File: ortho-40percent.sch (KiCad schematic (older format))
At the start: 28 parts, among them J1 USB-C_Receptacle-24, SW1 SW_NO_4-Pin, U1 U_TPD4E05U06DQAR, U2 U_ATmega32u4-MU, Y1 XTAL_4Lead

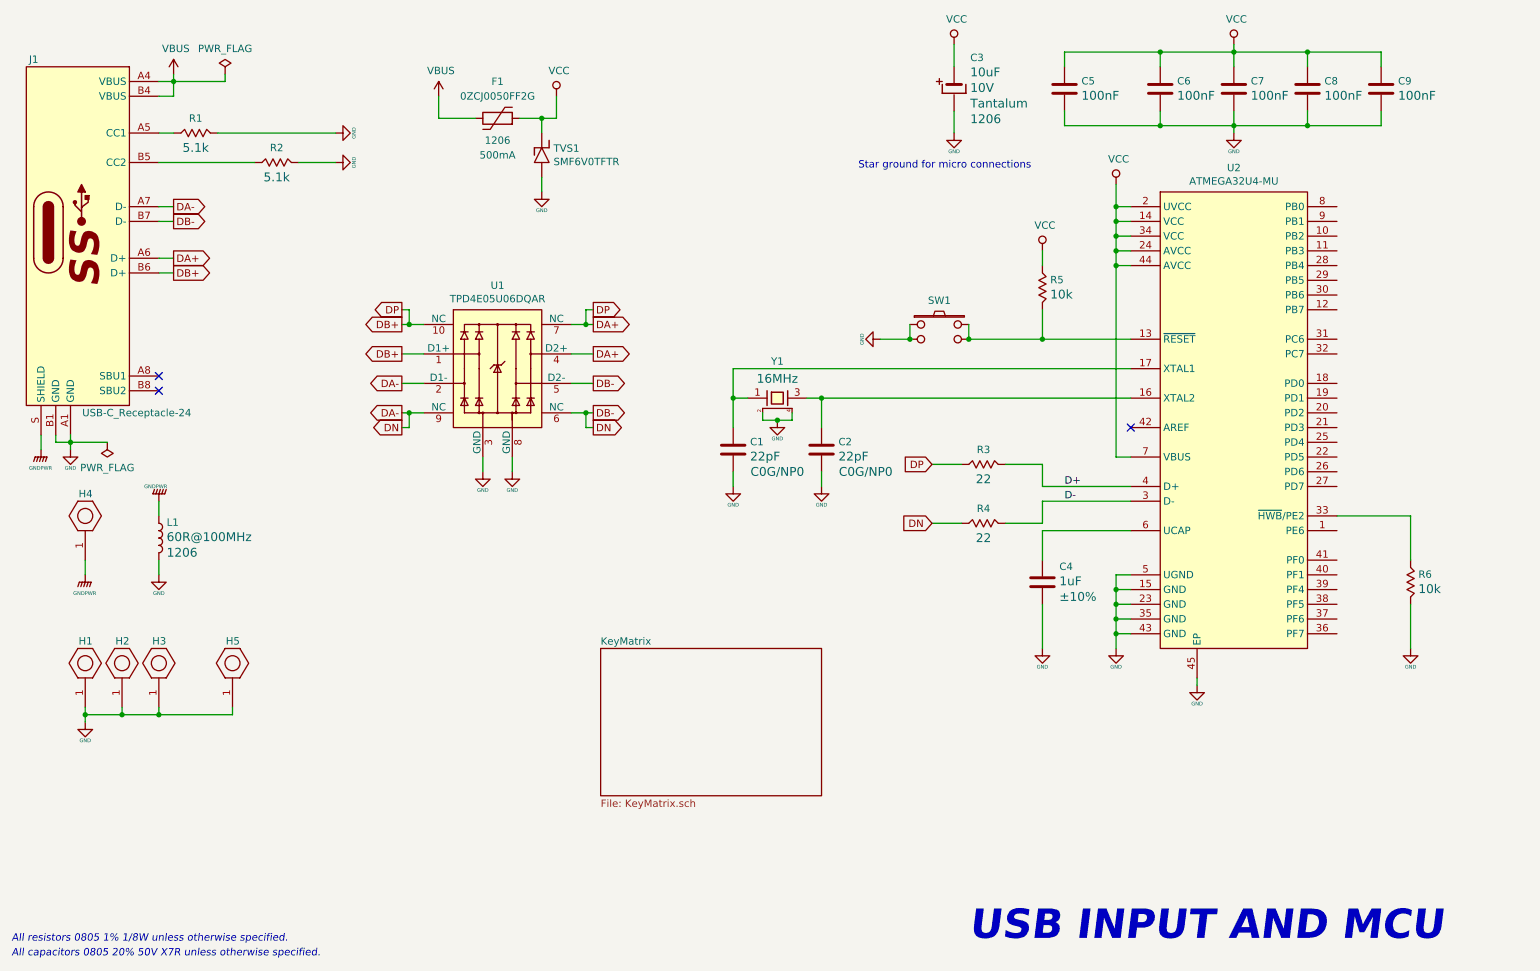
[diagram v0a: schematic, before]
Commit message: Routing Finished
All connections routed. Focusing on cleaning up for length optimization and minimal bottom plane cutting.
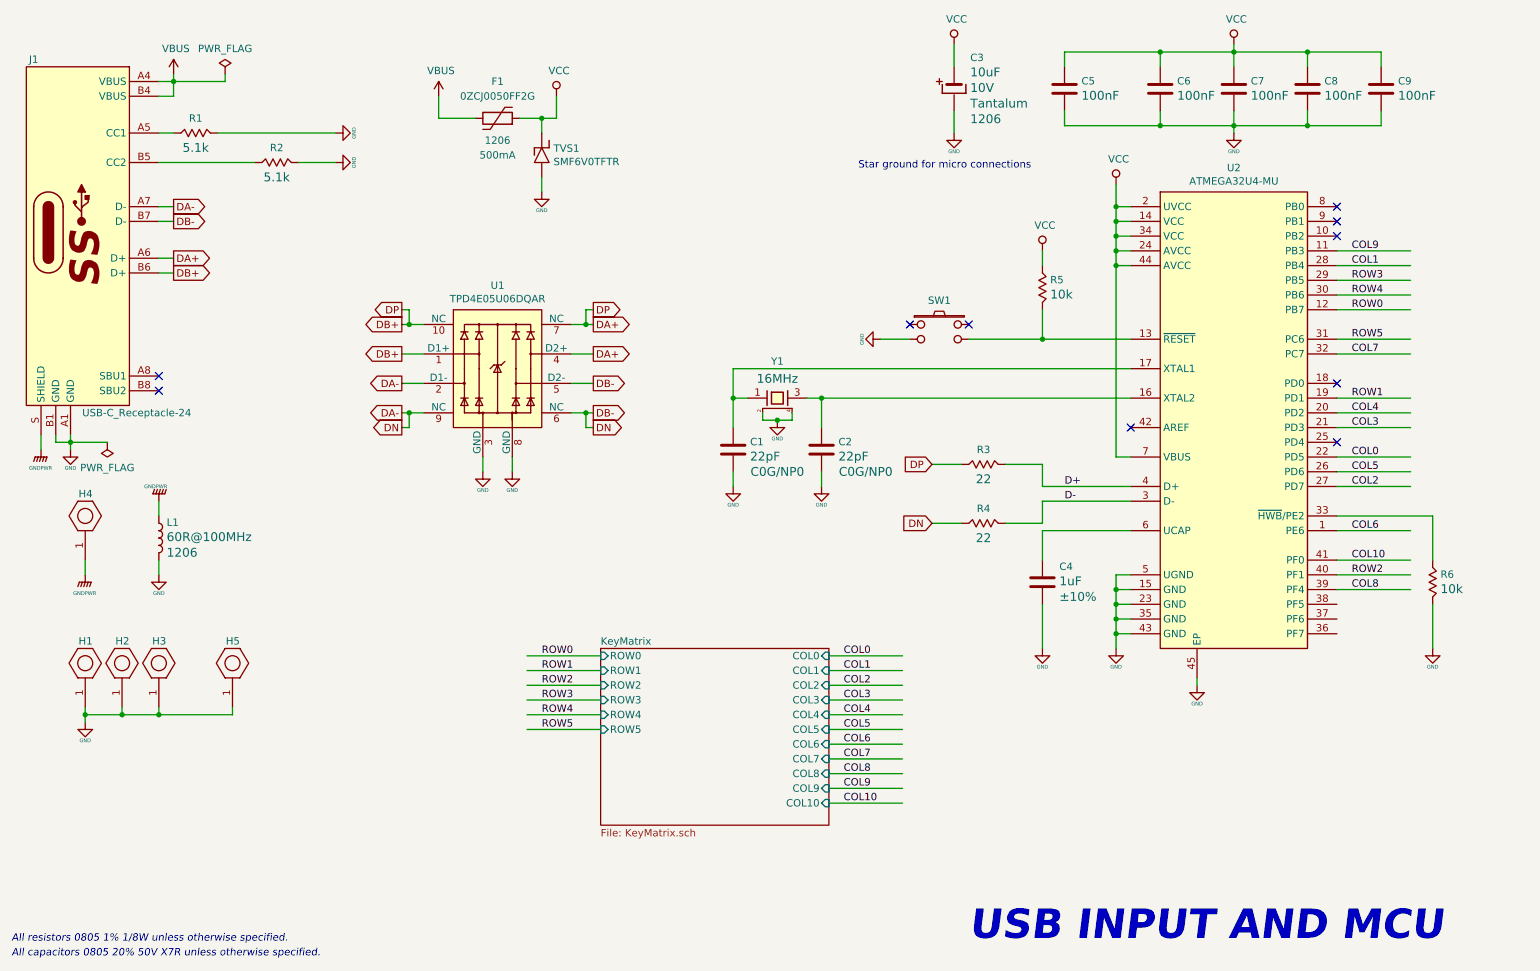
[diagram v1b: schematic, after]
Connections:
- net labels added: COL0, COL1, COL10, COL2, COL3, COL4, COL5, COL6, COL7, COL8, COL9, ROW0, ROW1, ROW2, ROW3, ROW4, ROW5
- wire segments 139 -> 171
- no-connect marks 3 -> 10
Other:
- moved on the sheet: R6
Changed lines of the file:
@@
 L master-vampire_General:R R6
 U 1 1 5F26A1E8
-P 10500 4550
-F 0 "R6" V 10447 4603 50  0000 L CNN
-F 1 "R" H 10500 4800 50  0001 C CNN
-F 2 "ortho-40percent:R_0805" H 10500 4620 50  0001 C CNN
-F 3 "" V 10500 4550 50  0000 C CNN
-F 4 "10k" V 10546 4603 60  0000 L CNN "Resistance"
-F 5 "1/8W" H 10900 4350 60  0001 C CNN "Power"
-F 6 "0805" H 10550 4350 60  0001 C CNN "Package"
-F 7 "1%" H 10800 4450 60  0001 C CNN "Tolerance"
-F 8 "RC0805FR-0710KL" H 11000 5150 50  0001 C CNN "MPN"
-F 9 "Yageo" H 11100 5250 50  0001 C CNN "Manufacturer"
-F 10 "DigiKey" H 11200 5350 50  0001 C CNN "Supplier"
-F 11 "311-10.0KCRCT-ND" H 11300 5450 50  0001 C CNN "Supplier PN"
-	1    10500 4550
+P 10650 4550
+F 0 "R6" V 10597 4603 50  0000 L CNN
+F 1 "R" H 10650 4800 50  0001 C CNN
+F 2 "ortho-40percent:R_0805" H 10650 4620 50  0001 C CNN
+F 3 "" V 10650 4550 50  0000 C CNN
+F 4 "10k" V 10696 4603 60  0000 L CNN "Resistance"
+F 5 "1/8W" H 11050 4350 60  0001 C CNN "Power"
+F 6 "0805" H 10700 4350 60  0001 C CNN "Package"
+F 7 "1%" H 10950 4450 60  0001 C CNN "Tolerance"
+F 8 "RC0805FR-0710KL" H 11150 5150 50  0001 C CNN "MPN"
+F 9 "Yageo" H 11250 5250 50  0001 C CNN "Manufacturer"
+F 10 "DigiKey" H 11350 5350 50  0001 C CNN "Supplier"
+F 11 "311-10.0KCRCT-ND" H 11450 5450 50  0001 C CNN "Supplier PN"
+	1    10650 4550
 	0    1    1    0
 $EndComp
@@
 L power:GND #PWR024
 U 1 1 5F273643
-P 10500 5000
-F 0 "#PWR024" H 10500 4750 50  0001 C CNN
-F 1 "GND" H 10500 4875 25  0000 C CNN
-F 2 "" H 10500 5000 50  0001 C CNN
-F 3 "" H 10500 5000 50  0001 C CNN
-	1    10500 5000
-	1    0    0    -1
-$EndComp
-Wire Wire Line
-	10000 4100 10500 4100
-Wire Wire Line
-	10500 4100 10500 4400
-Wire Wire Line
-	10500 4700 10500 5000
+P 10650 5000
+F 0 "#PWR024" H 10650 4750 50  0001 C CNN
+F 1 "GND" H 10650 4875 25  0000 C CNN
+F 2 "" H 10650 5000 50  0001 C CNN
+F 3 "" H 10650 5000 50  0001 C CNN
+	1    10650 5000
+	1    0    0    -1
+$EndComp
+Wire Wire Line
+	10650 4100 10650 4400
+Wire Wire Line
+	10650 4700 10650 5000
 Wire Wire Line
 	8600 4200 8000 4200
@@
 	5900 3100 8600 3100
 NoConn ~ 8600 3500
-Wire Wire Line
-	8000 2900 7500 2900
-Connection ~ 8000 2900
 $Comp
 L power:GND #PWR016
@@
 	0    1    1    0
 $EndComp
-Wire Wire Line
-	6900 2900 7100 2900
-Wire Wire Line
-	7500 2800 7500 2900
-Connection ~ 7500 2900
-Wire Wire Line
-	7100 2800 7100 2900
-Connection ~ 7100 2900
 $Comp
 L power:VCC #PWR022
@@
 	7400 1050 7400 900
 $Sheet
-S 5000 5000 1500 1000
+S 5000 5000 1550 1200
 U 5F33A928
 F0 "KeyMatrix" 50
 F1 "KeyMatrix.sch" 50
+F2 "ROW0" I L 5000 5050 50
+F3 "ROW1" I L 5000 5150 50
+F4 "ROW2" I L 5000 5250 50
+F5 "ROW3" I L 5000 5350 50
+F6 "ROW4" I L 5000 5450 50
+F7 "ROW5" I L 5000 5550 50
+F8 "COL0" I R 6550 5050 50
+F9 "COL1" I R 6550 5150 50
+F10 "COL2" I R 6550 5250 50
+F11 "COL3" I R 6550 5350 50
+F12 "COL4" I R 6550 5450 50
+F13 "COL5" I R 6550 5550 50
+F14 "COL6" I R 6550 5650 50
+F15 "COL7" I R 6550 5750 50
+F16 "COL8" I R 6550 5850 50
+F17 "COL9" I R 6550 5950 50
+F18 "COL10" I R 6550 6050 50
 $EndSheet
 $Comp
@@
 Wire Wire Line
 	1650 3600 1400 3600
+Wire Wire Line
+	10000 2600 10500 2600
+Wire Wire Line
+	10500 2700 10000 2700
+Wire Wire Line
+	10000 2900 10500 2900
+Wire Wire Line
+	10000 3900 10500 3900
+Wire Wire Line
+	10500 3300 10000 3300
+Wire Wire Line
+	10000 3400 10500 3400
+Wire Wire Line
+	10500 3500 10000 3500
+Wire Wire Line
+	10000 3800 10500 3800
+Wire Wire Line
+	10500 4500 10000 4500
+Wire Wire Line
+	10000 3000 10500 3000
+Text Label 10100 2700 0    50   ~ 0
+ROW0
+Text Label 10100 3300 0    50   ~ 0
+ROW1
+Text Label 10100 4500 0    50   ~ 0
+ROW2
+Text Label 10100 2500 0    50   ~ 0
+ROW3
+Text Label 10100 2600 0    50   ~ 0
+ROW4
+Text Label 10100 2900 0    50   ~ 0
+ROW5
+Wire Wire Line
+	4500 5050 5000 5050
+Wire Wire Line
+	4500 5150 5000 5150
+Wire Wire Line
+	5000 5250 4500 5250
+Wire Wire Line
+	4500 5350 5000 5350
+Wire Wire Line
+	5000 5450 4500 5450
+Wire Wire Line
+	4500 5550 5000 5550
+Text Label 4600 5050 0    50   ~ 0
+ROW0
+Text Label 4600 5150 0    50   ~ 0
+ROW1
+Text Label 4600 5250 0    50   ~ 0
+ROW2
+Text Label 4600 5350 0    50   ~ 0
+ROW3
+Text Label 4600 5450 0    50   ~ 0
+ROW4
+Text Label 4600 5550 0    50   ~ 0
+ROW5
+Wire Wire Line
+	10500 2500 10000 2500
+Wire Wire Line
+	10000 2400 10500 2400
+Wire Wire Line
+	10000 2300 10500 2300
+NoConn ~ 10000 2000
+NoConn ~ 10000 2100
+NoConn ~ 10000 2200
+Wire Wire Line
+	10500 3700 10000 3700
+Text Label 10100 3700 0    50   ~ 0
+COL0
+Text Label 10100 2400 0    50   ~ 0
+COL1
+Text Label 10100 3900 0    50   ~ 0
+COL2
+Text Label 10100 3500 0    50   ~ 0
+COL3
+Text Label 10100 3400 0    50   ~ 0
+COL4
+Text Label 10100 3800 0    50   ~ 0
+COL5
+Text Label 10100 4200 0    50   ~ 0
+COL6
+Text Label 10100 3000 0    50   ~ 0
+COL7
+Text Label 10100 4600 0    50   ~ 0
+COL8
+Text Label 10100 2300 0    50   ~ 0
+COL9
+Text Label 10100 4400 0    50   ~ 0
+COL10
+Wire Wire Line
+	10500 4600 10000 4600
+Wire Wire Line
+	10000 4100 10650 4100
+Wire Wire Line
+	10500 4200 10000 4200
+Wire Wire Line
+	10500 4400 10000 4400
+Wire Wire Line
+	6550 5150 7050 5150
+Wire Wire Line
+	7050 5250 6550 5250
+Wire Wire Line
+	6550 5350 7050 5350
+Wire Wire Line
+	7050 5450 6550 5450
+Wire Wire Line
+	6550 5550 7050 5550
+Wire Wire Line
+	7050 5650 6550 5650
+Wire Wire Line
+	6550 5750 7050 5750
+Text Label 6650 5150 0    50   ~ 0
+COL1
+Text Label 6650 5250 0    50   ~ 0
+COL2
+Text Label 6650 5350 0    50   ~ 0
+COL3
+Text Label 6650 5450 0    50   ~ 0
+COL4
+Text Label 6650 5550 0    50   ~ 0
+COL5
+Text Label 6650 5650 0    50   ~ 0
+COL6
+Text Label 6650 5750 0    50   ~ 0
+COL7
+Text Label 6650 5850 0    50   ~ 0
+COL8
+Wire Wire Line
+	7050 5850 6550 5850
+Text Label 6650 5950 0    50   ~ 0
+COL9
+Text Label 6650 6050 0    50   ~ 0
+COL10
+Wire Wire Line
+	7050 5950 6550 5950
+Wire Wire Line
+	7050 6050 6550 6050
+Wire Wire Line
+	7050 5050 6550 5050
+Text Label 6650 5050 0    50   ~ 0
+COL0
+Wire Wire Line
+	7500 2900 8000 2900
+Connection ~ 8000 2900
+Wire Wire Line
+	7100 2900 6900 2900
+NoConn ~ 7500 2800
+NoConn ~ 7100 2800
+NoConn ~ 10000 3200
+NoConn ~ 10000 3600
 $EndSCHEMATC

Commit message: Electrical Finished
All electrical completed, refdes placed. Beginning to place silkscreen logos and other branding items.
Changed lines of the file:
@@
 Wire Wire Line
 	10500 3700 10000 3700
+Text Label 10100 2400 0    50   ~ 0
+COL0
+Text Label 10100 3900 0    50   ~ 0
+COL1
+Text Label 10100 3800 0    50   ~ 0
+COL2
 Text Label 10100 3700 0    50   ~ 0
-COL0
-Text Label 10100 2400 0    50   ~ 0
-COL1
-Text Label 10100 3900 0    50   ~ 0
-COL2
+COL3
 Text Label 10100 3500 0    50   ~ 0
-COL3
+COL4
 Text Label 10100 3400 0    50   ~ 0
-COL4
-Text Label 10100 3800 0    50   ~ 0
 COL5
 Text Label 10100 4200 0    50   ~ 0
